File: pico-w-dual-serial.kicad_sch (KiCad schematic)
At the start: 65 parts, among them J1 DB9_Male, J2 DB9_Male, J3 RAPC722X, SW1 Mode Button, U1 PicoW, U2 MAX3232, U3 LM7805_TO220

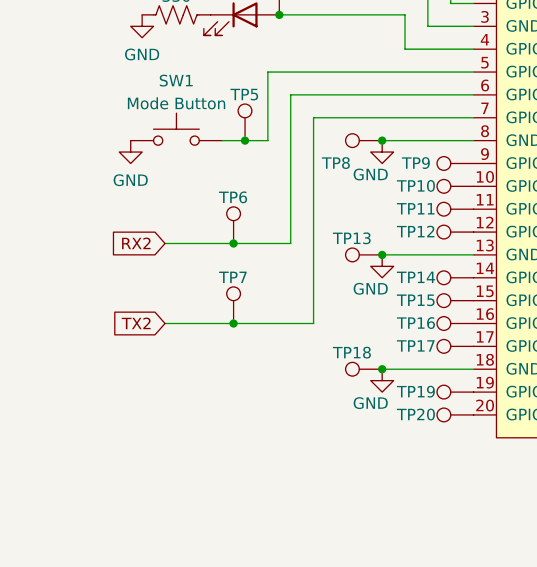
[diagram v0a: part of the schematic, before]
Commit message: fix reversed TX2/RX2
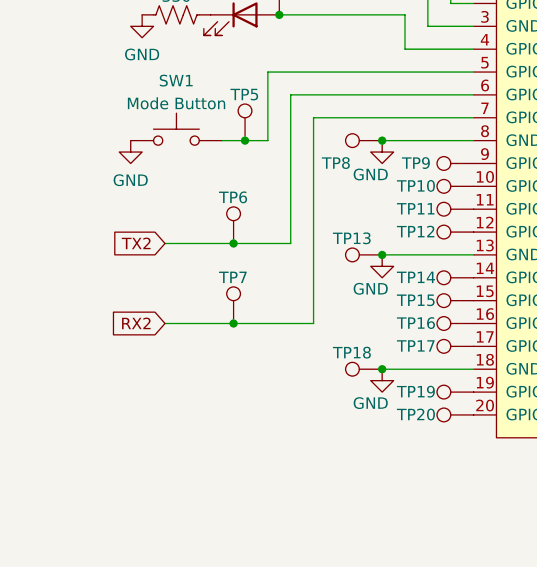
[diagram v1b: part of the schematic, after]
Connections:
- net RX2: now also TP7.1, U1.7 (GPIO5); no longer TP6.1, U1.6 (GPIO4)
- net TX2: now also TP6.1, U1.6 (GPIO4); no longer TP7.1, U1.7 (GPIO5)
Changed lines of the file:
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@@
+    (stroke (width 0) (type default))
+  )
+  (wire (pts (xy 30.48 80.01) (xy 38.1 80.01))
     (stroke (width 0) (type default))
   )
@@
     (stroke (width 0) (type default))
   )
-  (wire (pts (xy 30.48 80.01) (xy 38.1 80.01))
-    (stroke (width 0) (type default))
-  )
   (wire (pts (xy 62.23 44.45) (xy 62.23 35.56))
     (stroke (width 0) (type default))
@@
     (effects (font (size 1.27 1.27)) (justify right))
     (property "Intersheetrefs" "${INTERSHEET_REFS}" (at 150.1363 78.6606 0)
+      (effects (font (size 1.27 1.27)) (justify right) hide)
+    )
+  )
+  (global_label "RX2" (shape input) (at 30.48 80.01 180) (fields_autoplaced)
+    (effects (font (size 1.27 1.27)) (justify right))
+    (property "Intersheetrefs" "${INTERSHEET_REFS}" (at 24.46 80.01 0)
       (effects (font (size 1.27 1.27)) (justify right) hide)
     )
@@
     )
   )
-  (global_label "RX2" (shape input) (at 30.48 71.12 180) (fields_autoplaced)
-    (effects (font (size 1.27 1.27)) (justify right))
-    (property "Intersheetrefs" "${INTERSHEET_REFS}" (at 24.46 71.12 0)
-      (effects (font (size 1.27 1.27)) (justify right) hide)
-    )
-  )
   (global_label "RX1R" (shape input) (at 198.12 78.74 0) (fields_autoplaced)
     (effects (font (size 1.27 1.27)) (justify left))
@@
     )
   )
-  (global_label "TX2" (shape input) (at 30.48 80.01 180) (fields_autoplaced)
-    (effects (font (size 1.27 1.27)) (justify right))
-    (property "Intersheetrefs" "${INTERSHEET_REFS}" (at 24.7624 80.01 0)
-      (effects (font (size 1.27 1.27)) (justify right) hide)
-    )
+  (global_label "TX2" (shape input) (at 30.48 71.12 180) (fields_autoplaced)
+    (effects (font (size 1.27 1.27)) (justify right))
+    (property "Intersheetrefs" "${INTERSHEET_REFS}" (at 24.7624 71.12 0)
+      (effects (font (size 1.27 1.27)) (justify right) hide)
+    )

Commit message: new pic, better BOM
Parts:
- U2: Alternate (none) -> ADM3202 ANZ compatible and cheaper
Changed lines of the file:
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@@
+      (effects (font (size 1.27 1.27)) hide)
+    )
+    (property "Alternate" "ADM3202 ANZ compatible and cheaper" (at 176.53 66.04 0)
       (effects (font (size 1.27 1.27)) hide)
     )
